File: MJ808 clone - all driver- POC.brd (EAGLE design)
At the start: 35.5 x 35.5 mm, 38 parts, among them IC1 ATTINY4313-MMH, IC2 PRQV8.00CR1510Y00L, IC6 MCP2515, IC7 MAX16820, IC8 MCP2561-2, IC9 TPS709-Q1, K1 CRTL, Q1 PMV213SN,215, X1 22-23-2021, X2 22-23-2021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

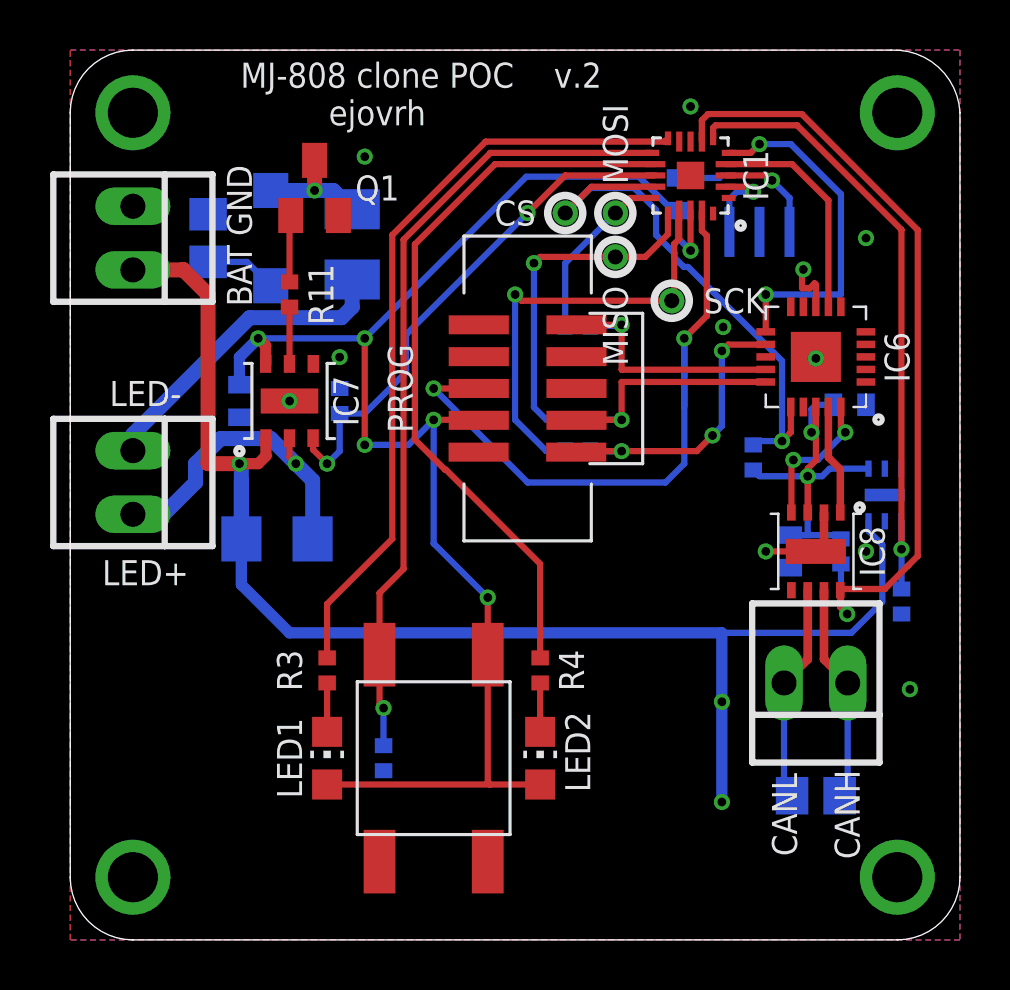
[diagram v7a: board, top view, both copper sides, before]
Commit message: - added passives xls calculator, added XLampXML2 datasheet, VLS6045EX-150M Inductor inductor - replaced LDO - updated BOM - recreated gerbers
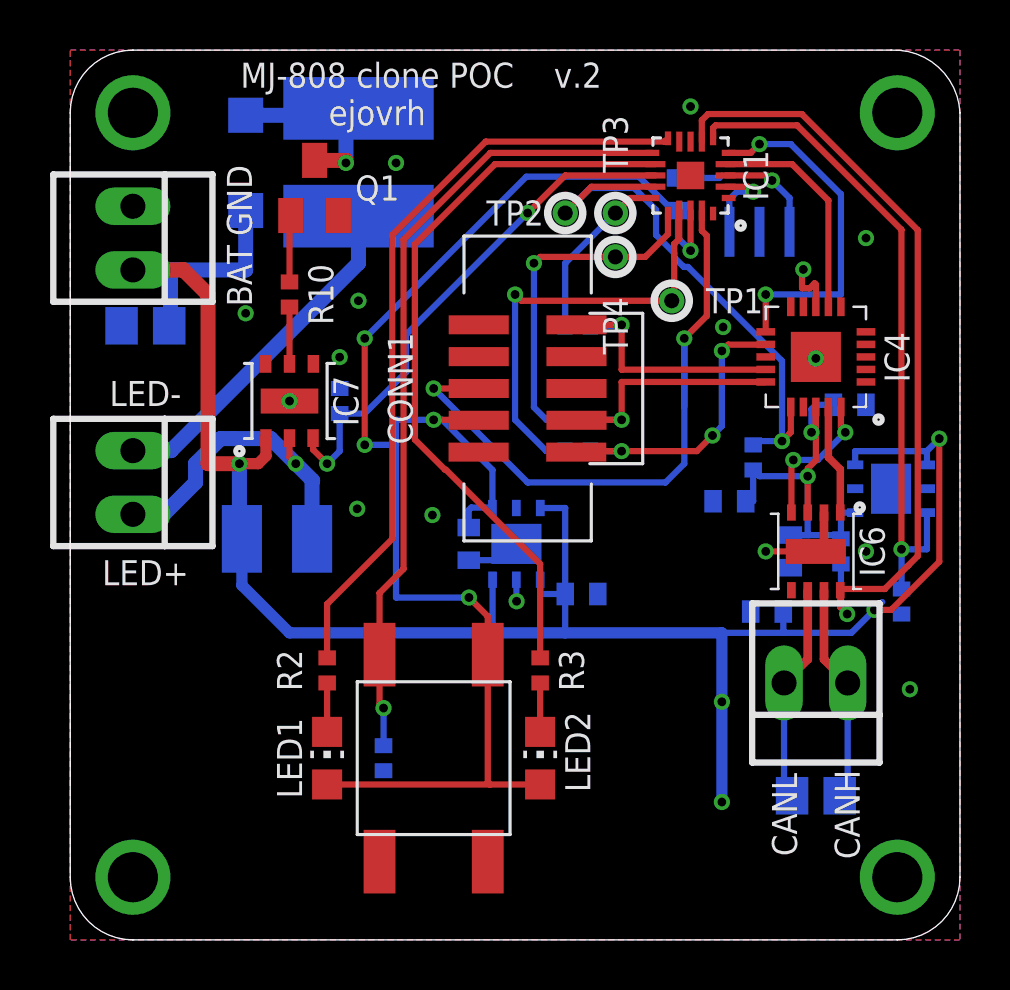
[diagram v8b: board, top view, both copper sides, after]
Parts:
- removed IC8: MCP2561-2, MCP2561-2 - High-Speed CAN Transceiver:DFN10
- removed IC9: TPS709-Q1, TPS709-q1 5V LDO:WSON6
- added C2, C3: 1μF, rcl:C0402
- added C4: 0.1μF, rcl:C0402
- added IC3, IC5: LP38693SD-5.0/NOPB, LP38693 5V LDO:WSON6
- added IC4: MCP2515, MCP2515-I-ML - Standalonce CAN Controller with SPI Interface:QFN20
- C5: value 0.1μF -> 1μF
- C6: value 47μF / 15V+ -> 1μF; device rcl:C0805 -> rcl:C0402
- C7: value 1μF -> 0.1μF
- C8: value 0.1μF -> 47μF / 15V+; device rcl:C0402 -> rcl:C0805
- IC6: value MCP2515 -> MCP2561-2; device MCP2515-I-ML - Standalonce CAN Controller with SPI Interface:QFN20 -> MCP2561-2 - High-Speed CAN Transceiver:DFN10
- L1: value AISC-1210HS-330K-T2 -> VLS6045EX-150M-CA; device eagle-ltspice:L3225M -> SparkFun-Coils:SRN6045
- LED1: value LTST-C281KRKT -> LTST-C170KRKT
- LED2: value LTST-C281KGKT -> LTST-C170KGKT
- R10: value 0.25 / 2W -> 10k; device rcl:R1206 -> rcl:R0402
- R11: value 10k -> 0.15 / 1W; device rcl:R0402 -> rcl:R1210
- R5: value 10k -> 330
- R9: value 330 -> 10k
- moved C8 27.3 mm to (3.00, 24.5), turned to 0 degrees
- moved C6 26.8 mm to (27.8, 13.1), turned to 0 degrees
- moved C7 22.8 mm to (28.8, 15.5)
- moved R9 14.8 mm to (33.2, 13.5), turned to 90 degrees
- moved R5 14.2 mm to (20.2, 19.5), turned to 0 degrees
- moved R4 13.4 mm to (10.8, 21.5), flipped to the bottom
- moved R2 10.8 mm to (10.2, 10.8), flipped to the top
- moved R10 9.76 mm to (8.75, 25.8), flipped to the top, turned to 90 degrees
- moved R11 9.76 mm to (8.25, 16.0), flipped to the bottom, turned to 0 degrees
- moved R3 8.50 mm to (18.8, 10.8)
- moved IC6 7.76 mm to (29.8, 15.5)
- moved C5 6.15 mm to (26.3, 17.5), turned to 0 degrees
- moved R6 5.00 mm to (20.2, 24.5)
- moved R8 3.75 mm to (20.2, 20.8)
- moved L1 3.26 mm to (11.5, 31.0)
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- renumbered CS to TP2, MISO to TP4, MOSI to TP3, PROG to CONN1, SCK to TP1
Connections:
- new net VCC: IC7.VCC
- net 5V0: now also C2.1, IC3.4-OUT; no longer C7.1, IC7.VCC
- net 5V0_REG: now also C4.1, C7.1, IC4.VDD, IC5.4-OUT; no longer C8.1, IC8.VDD, IC9.OUT
- net CANH: now also IC6.CANH; no longer IC8.CANH
- net CANL: now also IC6.CANL; no longer IC8.CANL
- net CLOCKOUT: now also IC4.OSC1; no longer IC6.OSC1
- net CSN: now also R11.1; no longer R10.1
- net DIM_FRONT: now also R4.2; no longer R2.2
- net DIM_FRONT_GATE: now also R10.1; no longer R11.1
- net EN: now also IC5.3-EN, R9.2; no longer IC9.EN, R5.2
- net GATE: now also R10.2; no longer R11.2
- net GND: now also C2.2, C3.1, C4.2, IC3.2-GND, IC3.GND1, IC4.GND, IC4.GND6, IC5.2-GND, IC5.GND1, IC6.VSS, R4.1, R9.1; no longer IC6.GND6, IC8.GND, IC8.VSS, IC9.GND, IC9.GND1, R2.1, R5.1
- net GREEN_LED: now also R3.1; no longer R4.1
- net INT: now also IC4.!INT!; no longer IC6.!INT!
- net N$4: now also R2.2; no longer R3.2
- net N$5: now also R3.2; no longer R4.2
- net RED_LED: now also R2.1; no longer R3.1
- net RXCAN: now also IC4.RXCAN, IC6.RXD; no longer IC6.RXCAN, IC8.RXD
- net SCK: now also IC4.SCK, R5.1; no longer IC6.SCK, R6.1
- net SI: now also IC4.SI, R6.1; no longer IC6.SI, R8.1
- net SO: now also IC4.SO, R8.1; no longer IC6.SO, R9.1
- net SPI_MISO: now also R8.2; no longer R9.2
- net SPI_MOSI: now also R6.2; no longer R8.2
- net SPI_SCK: now also R5.2; no longer R6.2
- net SPI_SS: now also IC4.!CS!; no longer IC6.!CS!
- net STBY: now also IC6.STBY; no longer IC8.STBY
- net TXCAN: now also IC4.TXCAN, IC6.TXD; no longer IC6.TXCAN, IC8.TXD
- net VBAT: now also C3.2, C8.1, IC3.1-IN, IC3.3-EN, IC3.6-IN, IC5.1-IN, IC5.6-IN, R11.2; no longer IC9.IN, R10.2
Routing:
- net VBAT: track 63.8 -> 85.2 mm, vias 3 -> 5
- net DIM_BRAKE_DRAIN: track 4.76 -> 7.86 mm
- net GND: track 8.62 -> 11.7 mm, vias 15 -> 20
- net LED+: track 12.6 -> 14.0 mm
- net EN: track 25.2 -> 26.5 mm
- net 5V0: track 59.9 -> 60.6 mm, vias 6 -> 5
- net 5V0_REG: track 17.4 -> 18.1 mm
